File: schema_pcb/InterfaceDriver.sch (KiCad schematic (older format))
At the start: 20 parts, among them K3 FautlPol, P5 +-10V, P6 InOut, Q1 NPN, U6 LM358, U7 74HC14

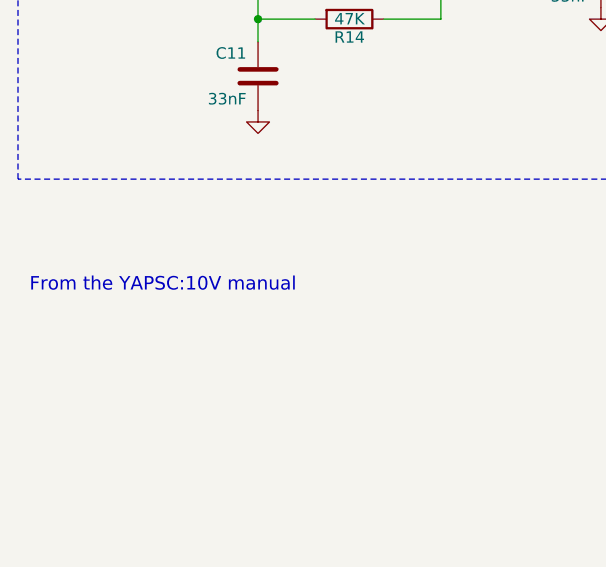
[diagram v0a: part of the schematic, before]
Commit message: Removed cutout from manual in InterfaceDriver
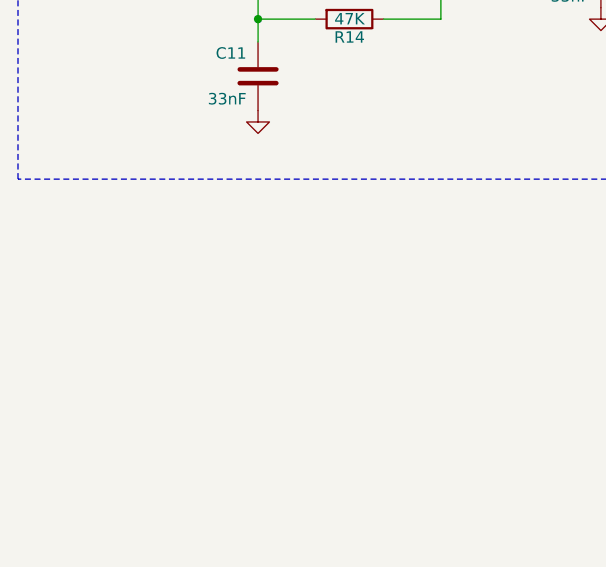
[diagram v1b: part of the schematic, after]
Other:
- note removed: "From the YAPSC:10V manual"
